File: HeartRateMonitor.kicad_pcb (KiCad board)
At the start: 2 copper layers, 30 x 46.5 mm, 66 parts, among them J1 USB_C_Receptacle_USB2.0, J2 SWD, J3 Conn_01x08_Pin, U1 CH340E, U10 TLV9301, U2 TLV9301, U3 TLV62130, U4 STM32G030F6Px, U5 TPS60403, U6 TLV9301, U7 TLV9301, U8 TLV9301, U9 AD5272BCP

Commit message: 0.9 (?)
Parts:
- moved C16 0.92 mm to (111.9, 111.8)
- moved C12 0.92 mm to (105.0, 125.5)
- moved C13 0.92 mm to (106.6, 125.5)
- moved C19 0.92 mm to (115.9, 117.5)
- moved R15 0.92 mm to (103.0, 125.5)
- moved R21 0.92 mm to (115.8, 115.8)
- moved U6 0.92 mm to (104.0, 121.8)
- moved U7 0.92 mm to (104.1, 113.5)
- moved C14 0.92 mm to (107.5, 114.8)
- moved C15 0.92 mm to (103.1, 117.2)
- moved C18 0.92 mm to (115.8, 119.1)
- moved C20 0.92 mm to (113.5, 121.7)
- moved R14 0.92 mm to (106.6, 122.4)
- moved R16 0.92 mm to (106.6, 118.8)
- moved R17 0.92 mm to (105.1, 117.2)
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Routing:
- net +3V3: track 32.0 -> 166.7 mm, vias 4 -> 9
- net -3V3: track 0.00 -> 84.2 mm, vias 0 -> 5
- net /HIGH_PH: track 0.00 -> 27.2 mm, vias 0 -> 2
- net Net-(D2-K): track 12.7 -> 33.2 mm, vias 0 -> 1
- net /LOW_PH: track 0.00 -> 18.1 mm, vias 0 -> 2
- net GND: track 24.1 -> 41.1 mm, vias 15 -> 29
- net /AMP_PH: track 0.00 -> 16.6 mm
- net /SCR_DATA: track 0.00 -> 14.4 mm
- net /SCR_SCK: track 0.00 -> 12.5 mm
- net Net-(D3-K): track 13.5 -> 26.0 mm, vias 0 -> 1
- net /DIGIPOT_SCL: track 0.00 -> 11.2 mm
- net /DIGIPOT_SDA: track 0.00 -> 8.97 mm
- net Net-(U6--): track 0.00 -> 7.06 mm
- net /RAW_PH: track 3.96 -> 10.9 mm, vias 0 -> 1
- net /DIGIPOT_A: track 0.00 -> 5.89 mm
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
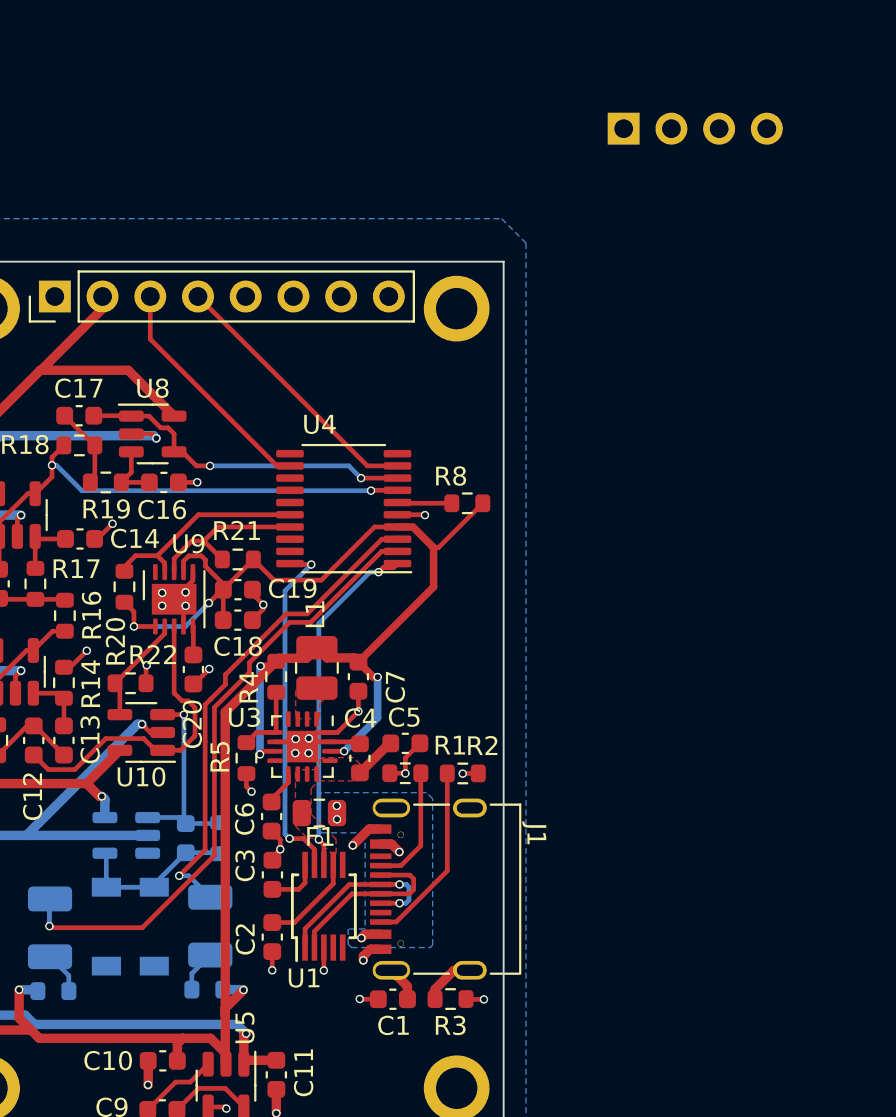
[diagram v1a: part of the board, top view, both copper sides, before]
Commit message: completed, left DRC unchecked
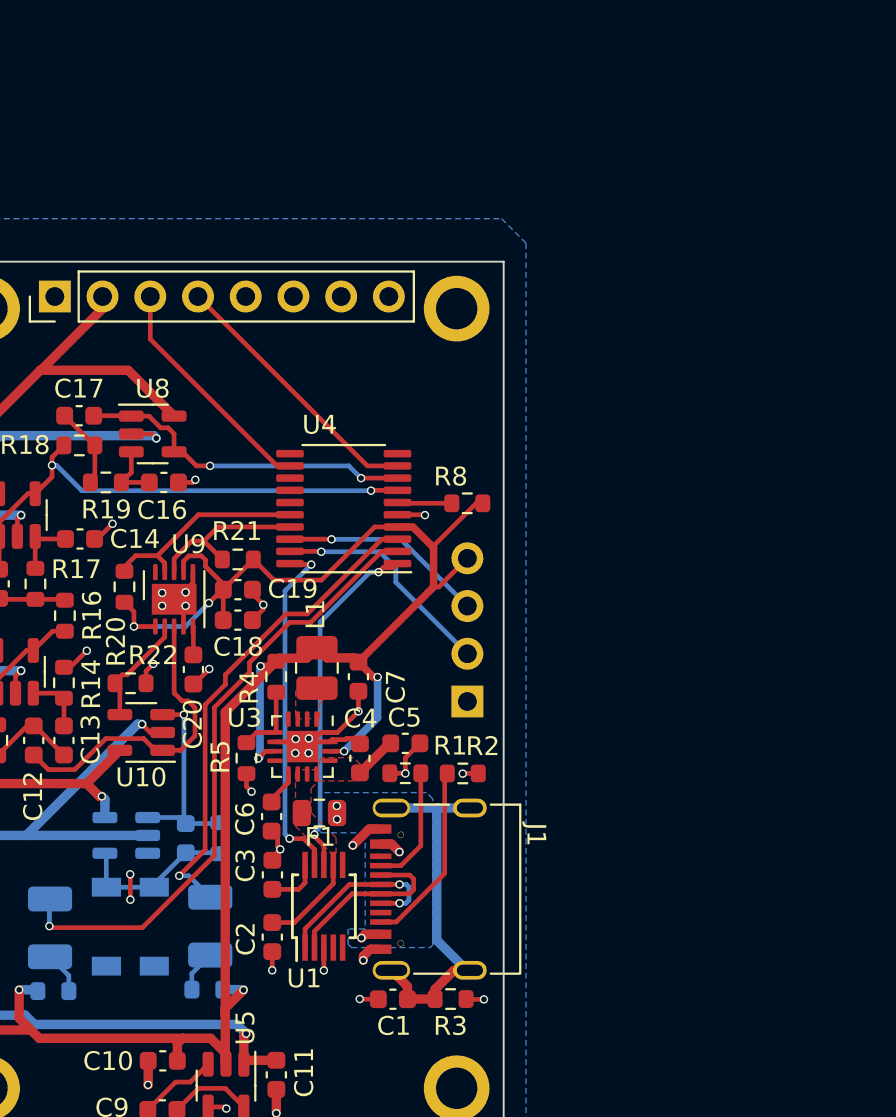
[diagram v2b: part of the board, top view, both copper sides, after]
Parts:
- moved J2 31.6 mm to (128.1, 123.4), turned to 0 degrees
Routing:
- net Net-(J1-SHIELD): track 4.69 -> 19.8 mm
- net Net-(J2-Pin_2): track 0.00 -> 12.1 mm, vias 0 -> 1
- net Net-(J2-Pin_3): track 0.00 -> 10.9 mm, vias 0 -> 1
- net +3V3: track 166.7 -> 169.6 mm
- net GND: track 41.1 -> 42.8 mm, vias 29 -> 31

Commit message: reconstruct
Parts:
- moved R12 60.1 mm to (124.0, 105.4), turned to -90 degrees
- moved R11 59.3 mm to (122.4, 105.4), turned to -90 degrees
- moved R7 56.9 mm to (117.9, 105.4), turned to -90 degrees
- moved R10 56.5 mm to (120.9, 105.4), turned to -90 degrees
- moved R6 56.1 mm to (116.3, 105.4), turned to -90 degrees
- moved R9 55.6 mm to (119.4, 105.4), turned to -90 degrees
- moved C9 19.4 mm to (102.4, 128.3), turned to 0 degrees
- moved U5 18.0 mm to (102.9, 130.8), turned to 180 degrees
- moved C11 17.4 mm to (103.1, 134.1)
- moved C10 13.3 mm to (101.6, 134.1), turned to -90 degrees
- moved C5 2.13 mm to (123.2, 124.2), turned to 180 degrees
- moved R4 1.77 mm to (116.3, 122.9)
- moved U2 0.62 mm to (110.5, 130.3), turned to -90 degrees
- moved R1 0.53 mm to (125.2, 127.5)
- moved R2 0.52 mm to (128.3, 127.5)
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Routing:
- net +3V3: track 169.6 -> 193.4 mm, vias 9 -> 14
- net Net-(D3-K): track 26.0 -> 46.1 mm, vias 1 -> 3
- net -3V3: track 84.2 -> 64.3 mm, vias 5 -> 9
- net /SCR_BLK: track 0.00 -> 16.6 mm, vias 0 -> 2
- net /SCR_CS: track 0.00 -> 14.9 mm, vias 0 -> 2
- net Net-(J1-SHIELD): track 19.8 -> 7.84 mm
- net /SCR_DC: track 0.00 -> 10.3 mm
- net /SCR_RES: track 0.00 -> 10.2 mm
- net Net-(D1-K): track 8.65 -> 0.00 mm
- net GND: track 42.8 -> 47.7 mm, vias 31 -> 29
- net Net-(J3-Pin_7): track 0.00 -> 4.70 mm
- net Net-(D2-K): track 33.2 -> 37.8 mm, vias 1 -> 3
- net /DIGIPOT_SCL: track 11.2 -> 15.8 mm
- net +5V: track 7.39 -> 11.9 mm
- net Net-(J3-Pin_6): track 0.00 -> 4.49 mm
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- added copper zone on B.Cu, net +3V3
- added copper zone on F.Cu, net +3V3
- added copper zone on F.Cu, net Net-(C17-Pad1)
- added copper zone on B.Cu, net Net-(D1-K)
- added copper zone on F.Cu, net Net-(U6-+)
- added copper zone on F.Cu, net Net-(U8-+)
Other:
- board text added: "0.0000 mm / 0.0000 mm"
- board text added: "0.3000 mm"
- board text added: "1.6000 mm"
- board text added: "2"
- board text added: "30.0000 mm x 46.5000 mm"
- board text added: "BOARD CHARACTERISTICS"
- board text added: "Board Thickness:"
- board text added: "Board overall dimensions:"
- board text added: "Castellated pads:"
- board text added: "Copper Finish:"
- board text added: "Copper Layer Count:"
- board text added: "Edge card connectors:"
- board text added: "Impedance Control:"
- board text added: "Min hole diameter:"
- board text added: "Min track/spacing:"
- board text added: "No"
- board text added: "None"
- board text added: "Plated Board Edge:"

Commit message: slightly modified filter and generated fabrication output
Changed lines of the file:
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@@
       (outputformat 1)
       (mirror false)
-      (drillshape 1)
+      (drillshape 0)
       (scaleselection 1)
-      (outputdirectory "")
+      (outputdirectory "Gerber/")
     )
   )
@@
       (effects (font (size 0.88 0.88) (thickness 0.13)) (justify mirror))
     )
-    (pad "1" smd roundrect (at -1.5375 0 270) (size 1.325 2.35) (layers "B.Cu" "B.Paste" "B.Mask") (roundrect_rratio 0.188679)
+    (pad "1" smd roundrect (at -1.5375 0 270) (size 1.325 2.35) (layers "B.Cu" "B.Paste" "B.Mask") (roundrect_rratio 0.1886792453)
       (net 39 "Net-(D3-K)") (pinfunction "K") (pintype "passive"))
-    (pad "2" smd roundrect (at 1.5375 0 270) (size 1.325 2.35) (layers "B.Cu" "B.Paste" "B.Mask") (roundrect_rratio 0.188679)
+    (pad "2" smd roundrect (at 1.5375 0 270) (size 1.325 2.35) (layers "B.Cu" "B.Paste" "B.Mask") (roundrect_rratio 0.1886792453)
       (net 40 "Net-(D3-A)") (pinfunction "A") (pintype "passive"))
     (model "${KICAD6_3DMODEL_DIR}/Capacitor_Tantalum_SMD.3dshapes/CP_EIA-3528-21_Kemet-B.wrl"
@@
       (effects (font (size 0.88 0.88) (thickness 0.13)) (justify mirror))
     )
-    (pad "1" smd roundrect (at -1.5375 0 270) (size 1.325 2.35) (layers "B.Cu" "B.Paste" "B.Mask") (roundrect_rratio 0.188679)
+    (pad "1" smd roundrect (at -1.5375 0 270) (size 1.325 2.35) (layers "B.Cu" "B.Paste" "B.Mask") (roundrect_rratio 0.1886792453)
       (net 41 "Net-(D2-K)") (pinfunction "K") (pintype "passive"))
-    (pad "2" smd roundrect (at 1.5375 0 270) (size 1.325 2.35) (layers "B.Cu" "B.Paste" "B.Mask") (roundrect_rratio 0.188679)
+    (pad "2" smd roundrect (at 1.5375 0 270) (size 1.325 2.35) (layers "B.Cu" "B.Paste" "B.Mask") (roundrect_rratio 0.1886792453)
       (net 42 "Net-(D2-A)") (pinfunction "A") (pintype "passive"))
     (model "${KICAD6_3DMODEL_DIR}/Capacitor_Tantalum_SMD.3dshapes/CP_EIA-3528-21_Kemet-B.wrl"

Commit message: finalize hardware
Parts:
- removed C13: 17.8uF, Capacitor_SMD:C_0603_1608Metric
- removed R10, R11, R12, R6, R7, R9: 0, Resistor_SMD:R_0603_1608Metric
- removed R15: 1K15, Resistor_SMD:R_0603_1608Metric
- removed U10, U7, U8: TLV9301, Package_TO_SOT_SMD:SOT-23-5
- added C21: 33uF, Capacitor_SMD:C_1206_3216Metric, F.Cu at (106.2, 114.3)
- added C22: 15uF, Capacitor_SMD:C_0402_1005Metric, F.Cu at (113.0, 116.6)
- added R25: 15K8, Resistor_SMD:R_0603_1608Metric, F.Cu at (112.5, 118.4)
- added R26: 3K92, Resistor_SMD:R_0603_1608Metric, F.Cu at (111.8, 116.1)
- added U11: LM2904, Package_SO:VSSOP-8_3.0x3.0mm_P0.65mm, F.Cu at (109.0, 129.8)
- C12: value 20.5uF -> 10uF
- C15: value 205nF -> 220nF
- C17: value 20.5uF -> 22uF
- C8, J2, R13: moved to F.Cu
- J1: footprint FP:TYPE-C-31-M-31 -> FP:TYPE-C-SMD_HX-TYPE-C-16PIN
- R14: value 4K22 -> 15K8
- R16, R18: value 2K37 -> 1K96
- R17, R19: value 3K24 -> 3K65
- U2: value TLV9301 -> LM2904; footprint Package_TO_SOT_SMD:SOT-23-5 -> Package_SO:VSSOP-8_3.0x3.0mm_P0.65mm; moved to F.Cu
- U6: value TLV9301 -> LM2904; footprint Package_TO_SOT_SMD:SOT-23-5 -> Package_SO:VSSOP-8_3.0x3.0mm_P0.65mm
- moved C19 20.5 mm to (100.8, 131.6), turned to -90 degrees
- moved R24 19.6 mm to (111.0, 119.4), turned to 90 degrees
- moved D3 16.0 mm to (114.3, 119.4), turned to 180 degrees
- moved U9 15.9 mm to (103.6, 131.0)
- moved C20 14.7 mm to (105.4, 133.9), turned to 0 degrees
- moved U6 13.6 mm to (109.0, 109.0), turned to 180 degrees
- moved C10 13.6 mm to (104.6, 120.9), turned to 90 degrees
- moved C18 13.5 mm to (106.2, 128.5), turned to 90 degrees
- moved U2 13.3 mm to (107.4, 117.3), turned to 0 degrees
- moved R20 13.1 mm to (101.1, 127.3)
- moved R4 12.4 mm to (113.0, 134.9), turned to -90 degrees
- moved R23 12.4 mm to (111.0, 127.5), turned to -90 degrees
- moved D2 11.7 mm to (114.3, 127.5), turned to 180 degrees
- moved D1 11.3 mm to (111.6, 121.4), turned to -90 degrees
- moved C9 10.9 mm to (102.1, 117.3)
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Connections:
- C12 pad 2: Net-(C12-Pad2) -> Net-(U2A-+)
- C14 pad 1: Net-(U7-+) -> Net-(U6A-+)
- C16 pad 1: Net-(U8-+) -> Net-(U6B-+)
- J3 pad 5: Net-(J3-Pin_5) -> /SCR_DC
- J3 pad 6: Net-(J3-Pin_6) -> /SCR_RES
- J3 pad 7: Net-(J3-Pin_7) -> /SCR_CS
- R14 pad 1: Net-(U6-+) -> Net-(U2A-+)
- R16 pad 1: Net-(U6--) -> Net-(U2B--)
- R17 pad 2: Net-(U7-+) -> Net-(U6A-+)
- R19 pad 2: Net-(U8-+) -> Net-(U6B-+)
- U2 pad 1: /RAW_PH -> Net-(U2A--)
- U2 pad 2: -3V3 -> Net-(U2A--)
- U2 pad 3: GND -> Net-(U2A-+)
- U2 pad 4: Net-(D1-K) -> -3V3
- U2 pad 5: +3V3 -> Net-(U2B-+)
- U6 pad 1: Net-(U6--) -> /HIGH_PH
- U6 pad 2: -3V3 -> /HIGH_PH
- U6 pad 3: Net-(U6-+) -> Net-(U6A-+)
- U6 pad 4: Net-(U6--) -> -3V3
- U6 pad 5: +3V3 -> Net-(U6B-+)
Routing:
- net +3V3: track 193.4 -> 157.8 mm, vias 14 -> 13
- net Net-(D3-K): track 46.1 -> 15.2 mm, vias 3 -> 1
- net -3V3: track 64.3 -> 36.8 mm, vias 9 -> 4
- net /DIGIPOT_SDA: track 10.5 -> 28.2 mm
- net Net-(D2-K): track 37.8 -> 20.5 mm, vias 3 -> 1
- net /DIGIPOT_SCL: track 15.8 -> 30.3 mm
- net GND: track 47.7 -> 37.2 mm
- net Net-(J1-SHIELD): track 7.84 -> 17.0 mm
- net Net-(U6--): track 8.21 -> 0.00 mm
- net Net-(U6A-+): track 0.00 -> 8.12 mm
- net Net-(U2A-+): track 0.00 -> 7.83 mm
- net Net-(D1-K): track 0.00 -> 7.56 mm, vias 0 -> 1
- net Net-(C21-Pad2): track 0.00 -> 7.21 mm
- net /AMP_PH: track 17.4 -> 24.2 mm
- net Net-(U6B-+): track 0.00 -> 6.12 mm
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- added copper zone on F.Cu, net /HIGH_PH
- added copper zone on F.Cu, net /LOW_PH
- added copper zone on F.Cu, net Net-(F1-Pad1)
- added copper zone on F.Cu, net Net-(J1-SHIELD)
- added copper zone on F.Cu, net Net-(U2A--)
- added copper zone on F.Cu, net Net-(U2B--)
- removed copper zone on B.Cu, net +3V3
- removed copper zone on F.Cu, net Net-(C17-Pad1)
- removed copper zone on F.Cu, net Net-(U6-+)
- removed copper zone on F.Cu, net Net-(U8-+)
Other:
- board text added: "0.1270 mm / 0.1270 mm"
- board text removed: "0.0000 mm / 0.0000 mm"

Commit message: Hardware Cleanup
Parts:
- removed the REF** at (127.5, 102.5)
- removed the REF** at (102.5, 144.0)
- removed the REF** at (102.5, 102.5)
- removed the REF** at (127.5, 144.0)
- added REF**: M2-MountingHole, FP:M2-MountingHole, F.Cu at (21.7, 68.0)
- added REF**: M2-MountingHole, FP:M2-MountingHole, F.Cu at (21.7, 26.5)
- added REF**: M2-MountingHole, FP:M2-MountingHole, F.Cu at (46.7, 26.5)
- added REF**: M2-MountingHole, FP:M2-MountingHole, F.Cu at (46.7, 68.0)
- added REF**: ESD-Logo_6.6x6mm_SilkScreen, Symbol:ESD-Logo_6.6x6mm_SilkScreen, B.Cu at (24.1, 48.2)
- added REF**: OSHW-Logo_5.7x6mm_SilkScreen, Symbol:OSHW-Logo_5.7x6mm_SilkScreen, B.Cu at (29.2, 57.9)
- moved R2 110.9 mm to (44.2, 53.8)
- moved C14 110.9 mm to (32.5, 35.0)
- moved C15 110.9 mm to (30.2, 35.8)
- moved C17 110.9 mm to (24.1, 35.8)
- moved C18 110.9 mm to (25.4, 52.5)
- moved C20 110.9 mm to (24.6, 57.9)
- moved L1 110.9 mm to (35.6, 51.2)
- moved R1 110.9 mm to (47.3, 53.8)
- moved R16 110.9 mm to (29.5, 38.0)
- moved R17 110.9 mm to (27.2, 35.8)
- moved R18 110.9 mm to (21.9, 36.5)
- moved R20 110.9 mm to (20.3, 51.2)
- moved R25 110.9 mm to (31.8, 42.4)
- moved U1 110.9 mm to (39.6, 61.7)
- moved U11 110.9 mm to (28.2, 53.8)
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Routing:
- net Net-(J1-SHIELD): track 17.0 -> 0.00 mm
- net GND: track 37.2 -> 38.7 mm, vias 29 -> 27
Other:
- board text added: "0"
- board text added: "0 mm"
- board text added: "0.01 mm"
- board text added: "0.02"
- board text added: "0.035 mm"
- board text added: "1"
- board text added: "1.465 mm"
- board text added: "3.3"
- board text added: "4.5"
- board text added: "B.Cu"
- board text added: "B.Mask"
- board text added: "B.Paste"
- board text added: "B.Silkscreen"
- board text added: "Bottom Silk Screen"
- board text added: "Bottom Solder Mask"
- board text added: "Bottom Solder Paste"
- board text added: "Color"
- board text added: "Dielectric 1"
- board text added: "Epsilon R"
- board text added: "F.Cu"
- board text added: "F.Mask"
- board text added: "F.Paste"
- board text added: "F.Silkscreen"
- board text added: "FR4"
- board text added: "Layer Name"
- board text added: "Loss Tangent"
- board text added: "Material"
- board text added: "Not specified"
- board text added: "Thickness (mm)"
- board text added: "Top Silk Screen"
- board text added: "Top Solder Mask"
- board text added: "Top Solder Paste"
- board text added: "Type"
- board text added: "copper"
- board text added: "core"
- board text added: "locked"
